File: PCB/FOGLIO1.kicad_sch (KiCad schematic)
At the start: 48 parts, among them J2 USB_C_Receptacle_PowerOnly_6P, J3 6871XX182122_687110182122, J5 Conn_01x03_Pin, J7 Conn_01x07_Pin, U1 TPD2E2U06DCK, U2 ADS131M08xPBS, U3 74LVC1G17, U4 LM27762, U5 AD7606

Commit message: Swap AD7606 for ADS131M08, rework analog front-end and USB input
Schematic-only changes; the PCB has not been updated from the schematic
yet. PCB/CHANGELOG-2026-09-28-ADC-swap.md has the per-part details: every
added/removed part with its pin-to-net list, the netlist diff (before ->
after) and the ERC counts.

1. ADC swap (FOGLIO1)
- Remove the AD7606 (U5) and parts that only served it: C29-C32, C45-C47,
  BUSY LED D3/R8 and the old 1x07 J7.
- Wire up the ADS131M08 (U2): internal 1.2 V reference with 100n on REFIN,
  XTAL2 no-connect, AINxN tied to GND.
- Per-channel divider + anti-alias RC (R61-R76 1.1k/1k, C48-C55 10n C0G):
  op-amp swing +-2.45 V -> +-1.17 V for the +-1.2 V ADC full scale,
  fc ~30 kHz. Channel 7 now digitises the sacrificial-sensor output Vsac.
- ADC supply: U7 TPS7A2033 LDO from +5V -> +3.3VA (AVDD), FB1 -> +3V3
  (DVDD, U3, pull-ups). 1.7 V headroom gives full PSRR, which a passive
  filter on raw VBUS could not.
- Clock from the STM32H7 (MCO2, 5.12 MHz, OSR 256 -> 10 kSPS):
  MCU_CLK -> U3 74LVC1G17 Schmitt buffer -> R80 33R -> CLKIN, with R79
  100k pull-down so CLKIN never floats.
- SPI: R81/R82 33R source terminations on DOUT/DRDY, R77/R78 10k pull-ups
  on CS and SYNC/RESET.
- New 2x06 J7 with GND next to CLK and SCLK.
- Vsac brought from the SENSORS sheet through a new sheet pin (plain wire
  on the root sheet).
- FOGLIO1 paper A4 -> A3. PWR_FLAG added on GND (pre-existing ERC error).

2. Op-amp section swap (FOGLIO2)
- U6 and U13, the two quads next to J3, now hold all 8 first stages
  (S1-S7 and S_sac); U11/U12 hold the 7 difference amps. The
  high-impedance sensor traces can now stay short and on F.Cu.
- Section order chosen from the J3/op-amp pad positions so the sensor
  traces can be routed without crossings.
- Spare section U12-D wired as a follower with +IN at GND (previously
  U13-D was left floating).
- Passive references, values and symbol UUIDs are unchanged, so the PCB
  footprints stay linked.

3. SENSORS sheet readability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
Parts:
- removed C21, C46, C47: 10u, Capacitor_SMD:C_0805_2012Metric, symbol Device:C
- removed C29, C30, C31, C32: 100n, Capacitor_SMD:C_0603_1608Metric, symbol Device:C_Small
- removed C45: 1u, Capacitor_SMD:C_0603_1608Metric, symbol Device:C
- removed D3: LED, LED_SMD:LED_0603_1608Metric, symbol Device:LED
- removed J7: Conn_01x07_Pin, Connector_PinHeader_2.54mm:PinHeader_1x07_P2.54mm_Vertical_SMD_Pin1Right, symbol Connector:Conn_01x07_Pin
- removed R8: 4.7k, Resistor_SMD:R_0603_1608Metric, symbol Device:R
- removed U5: AD7606, Package_QFP:LQFP-64_10x10mm_P0.5mm, symbol Analog_ADC:AD7606
- added C48, C49, C50, C51, C52, C53, C54, C55: 10n C0G, Capacitor_SMD:C_0603_1608Metric, symbol Device:C_Small
- added C58, C59: 100n, Capacitor_SMD:C_0603_1608Metric, symbol Device:C_Small
- added C60, C61: 1u, Capacitor_SMD:C_0603_1608Metric, symbol Device:C_Small
- added C62: 22u 16V, Capacitor_SMD:C_0603_1608Metric, symbol Device:C_Small
- added D1: SMF5.0A, Diode_SMD:D_SMF, symbol Diode:SMF5V0A
- added FB1: BLM18PG221SN1, Inductor_SMD:L_0603_1608Metric, symbol Device:FerriteBead_Small
- added FB2: BLM18KG102SN1, Inductor_SMD:L_0603_1608Metric, symbol Device:FerriteBead_Small
- added J7: Conn_02x06_Odd_Even, Connector_PinHeader_2.54mm:PinHeader_2x06_P2.54mm_Vertical_SMD, symbol Connector_Generic:Conn_02x06_Odd_Even
- added R61, R63, R65, R67, R69, R71, R73, R75: 1.1k, Resistor_SMD:R_0603_1608Metric, symbol Device:R_Small
- added R62, R64, R66, R68, R70, R72, R74, R76: 1k, Resistor_SMD:R_0603_1608Metric, symbol Device:R_Small
- added R77, R78: 10k, Resistor_SMD:R_0603_1608Metric, symbol Device:R_Small
- added R79: 100k, Resistor_SMD:R_0603_1608Metric, symbol Device:R_Small
- added R80, R81, R82: 33R, Resistor_SMD:R_0603_1608Metric, symbol Device:R_Small
- added U7: TPS7A2033PDBVR, Package_TO_SOT_SMD:SOT-23-5, symbol Regulator_Linear:TPS7A20xxxDBV
- U3: footprint (none) -> Package_TO_SOT_SMD:SOT-23-5
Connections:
- net +3V3: now also C36.1, U2.26 (DVDD), C58.1, FB1.2, R77.1, R78.1
- net +5V: now also C60.1, C62.1, D1.1 (A1), FB2.1, U7.1 (IN), U7.3 (EN); no longer C33.1, C34.1, R11.1, R12.1, U4.3 (VIN)
- net GND: now also C48.2, C49.2, C50.2, C51.2, C52.2, C53.2, C54.2, C55.2, C58.2, C59.2, C60.2, C61.2, C62.2, D1.2 (A2), J7.1 (Pin_1), J7.11 (Pin_11), J7.12 (Pin_12), J7.3 (Pin_3), J7.6 (Pin_6), R62.2, R64.2, R66.2, R68.2, R70.2, R72.2, R74.2, R76.2, R79.2, U7.2 (GND)
- net MCU_CLK: now also J7.2 (Pin_2), R79.1
- net Vout1: now also R61.1; no longer U2.29 (AIN0P)
- net Vout2: now also R63.1; no longer U2.32 (AIN1P)
- net Vout3: now also R65.1; no longer U2.1 (AIN2P)
- net Vout4: now also R67.1; no longer U2.4 (AIN3P)
- net Vout5: now also R69.1; no longer U2.5 (AIN4P)
- net Vout6: now also R71.1; no longer U2.8 (AIN5P)
- net Vout7: now also R73.1; no longer U2.9 (AIN6P)
- net Vsac: now also R75.1; no longer U2.12 (AIN7P)
- net at U2.14 (REFIN): now also C59.1
- net +3.3VA: now reaches C37.1, U2.15 (AVDD)
- net +3.3VA: now also C61.1, FB1.1, U7.5 (OUT)
- net ADC_SYNC_RESET: now reaches U2.16 (~{SYNC}/~{RESET})
- net ADC_SYNC_RESET: now also J7.10 (Pin_10), R78.2
- net ADC_CS: now reaches U2.17 (~{CS})
- net ADC_CS: now also J7.8 (Pin_8), R77.2
- net U2_DRDY: now reaches U2.18 (~{DRDY})
- net U2_DRDY: now also R82.1
- net ADC_SCLK: now reaches U2.19 (SCLK)
- net ADC_SCLK: now also J7.4 (Pin_4)
- net U2_DOUT: now reaches U2.20 (DOUT)
- net U2_DOUT: now also R81.1
- net ADC_MOSI: now reaches U2.21 (DIN)
- net ADC_MOSI: now also J7.5 (Pin_5)
- net at U2.23 (XTAL1/CLKIN): now also R80.1; no longer U3.4
- new net: R80.2, U3.4
- new net +5V_CP: C33.1, C34.1, FB2.2, R11.1, R12.1, U4.3 (VIN)
- new net ADC_DRDY: J7.9 (Pin_9), R82.2
- new net ADC_MISO: J7.7 (Pin_7), R81.2
- new net AIN0P: C48.1, R61.2, R62.1, U2.29 (AIN0P)
- new net AIN1P: C49.1, R63.2, R64.1, U2.32 (AIN1P)
- new net AIN2P: C50.1, R65.2, R66.1, U2.1 (AIN2P)
- new net AIN3P: C51.1, R67.2, R68.1, U2.4 (AIN3P)
- new net AIN4P: C52.1, R69.2, R70.1, U2.5 (AIN4P)
- new net AIN5P: C53.1, R71.2, R72.1, U2.8 (AIN5P)
- new net AIN6P: C54.1, R73.2, R74.1, U2.9 (AIN6P)
- new net AIN7P: C55.1, R75.2, R76.1, U2.12 (AIN7P)
- no-connect marks 16 -> 1
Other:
- note added: "+5V -> U7 TPS7A2033 -> +3.3VA (U2 AVDD) +3.3VA -> FB1 -> +3V3 (U2 DVDD, U3, pull-ups)"
- note added: "ADC INPUT DIVIDERS + ANTI-ALIAS (one row per ADS131M08 channel)"
- note added: "ADC SUPPLY (LDO + FERRITE)"
- note added: "J7 -> STM32H7 (3.3 V logic) MCU_CLK: 5.12 MHz from H7 MCO2 (PC9), 40-60 % duty -> U3 Schmitt buffer -> R80 -> ADC CLKIN (10 kSPS @ OSR 256) ADC_SCLK/MOSI/MISO/CS: SPI mode 1 (CPOL 0, CPHA 1), ~8 MHz, SPI clock from the same PLL as MCO2 (synchronous) ADC_DRDY: data ready, active low -> DMA read of 10 words ADC_SYNC_RESET: sync / reset (>= 2048 tCLKIN low), active low Fit 33R series R at the H7 sid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"
- note added: "R81/R82: place next to U2 (source termination)"
- note added: "Ratio 1.0k/(1.1k+1.0k) = 0.476 -> op-amp ±2.45 V maps to ±1.17 V (ADS131M08 FS ±1.2 V). Thevenin 524 Ω + 10 nF C0G -> fc ≈ 30 kHz. AINnN tied to GND at U2 (pseudo-differential). CH7 digitises the sacrificial-sensor output Vsac for diagnostics."
- note added: "USB INPUT: D1 TVS + PI FILTER VBUS (+5V) -> C62 -> FB2 -> +5V_CP (U4 VIN; C34/C33 are the U4-side caps) U7 (ADC LDO), D2/R7 and TP1 stay on +5V (connector side of FB2). Place D1 and C62 right at J2 VBUS/GND pins."
- note removed: "BUSY LED CHECK"
- note removed: "Vdrive = 3v3/5V uC CONVST = instant shoot of output SPI_MISO = bus MISO SPI SPI_CS= bus CS SPI SPI_SCK = bus CK SPI BUSY = if it has level high, the ADC is busy RESET = reset"
- moved on the sheet: C35, C36, C37, U2, U3

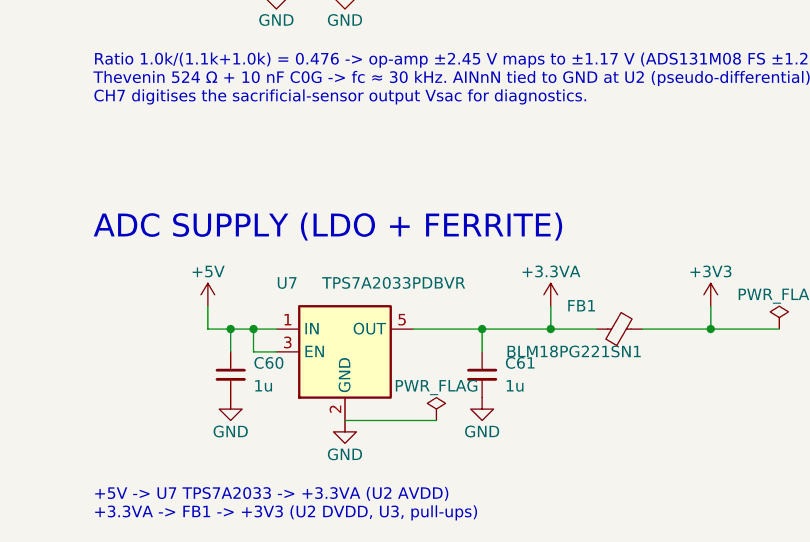
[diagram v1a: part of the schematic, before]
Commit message: Add MPNs to all parts, switch unavailable parts, add Mouser BOM
Schematic procurement pass, based on a Mouser Italia stock/price check
(2026-09-28). The netlist is unchanged and ERC is still at 0 errors.
Details are in PCB/CHANGELOG-2026-09-28-ADC-swap.md, Part 5.

Schematic (FOGLIO1, FOGLIO2):
- Every orderable part (123) now has MPN and Manufacturer fields. The
  old SnapEDA "MF" field on the op-amps is replaced by Manufacturer.
- Difference-amp resistors 5k -> 4.99k (R23, R25, R28, R30, R33, R35,
  R40, R41, R43, R45, R50, R51, R55, R60). Exact 5.0k only exists at
  0.1 %/25 ppm for about EUR 1.7. Both halves of each difference amp use
  the same 4.99k/10k pair, so the ratio still matches (gain 2.004).
- U7 TPS7A2033PDBVR (out of stock, 26-week lead) -> LP5907MFX-3.3/NOPB.
  Same SOT-23-5 pinout and footprint (IN 1, GND 2, EN 3, NC 4, OUT 5).
  The symbol is now Regulator_Linear:LP5907MFX-3.3.
- C62 -> Murata GRM219R61C226ME15K, 22 uF 16 V X5R, footprint
  changed to 0805 (the 0603 ZRB part was out of stock until mid-October).
- Precision parts, all 0.1 % / 25 ppm thin film:
  - 1M Rf and 1k: KOA RN73R
  - 4.99k, 10k, 1.1k: Yageo RT0603BRD
- Capacitor MPNs:
  - 15 pF C0G: Samsung CL10C150JB8NNNC (all Murata 0603 parts are NRND)
  - 10 nF: GRM1885C1H103JA01D
  - 100 nF: GRM188R72A104KA35D (previous part obsolete)
  - 1 uF: GRT188R71E105KE13D (previous part obsolete)
  - 4.7 uF: GRT188R61C475KE13D (previous part not orderable)
  - 10 uF 0805: GRJ21BR61E106KE01L
  - 220 nF: GRM188R71E224KA88D
- General-purpose resistors: Yageo RC0603FR-07; 105k is
  AC0603FR-07105KL because the RC part has no stock.

BOM (PCB/bom/BOM_Mouser_2026-09-28.csv):
- 35 lines, 124 parts per board. Each line has quantity, references,
  value, description, manufacturer, MPN, Mouser link, stock and EUR
  price at qty 10/100.
- Priced parts come to about EUR 49 per board at qty 10.

Open points:
- J5 has no MPN yet (needs a 1x03 2.54 mm SMD alternating-pin header).
- Stock not checked for D2, J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
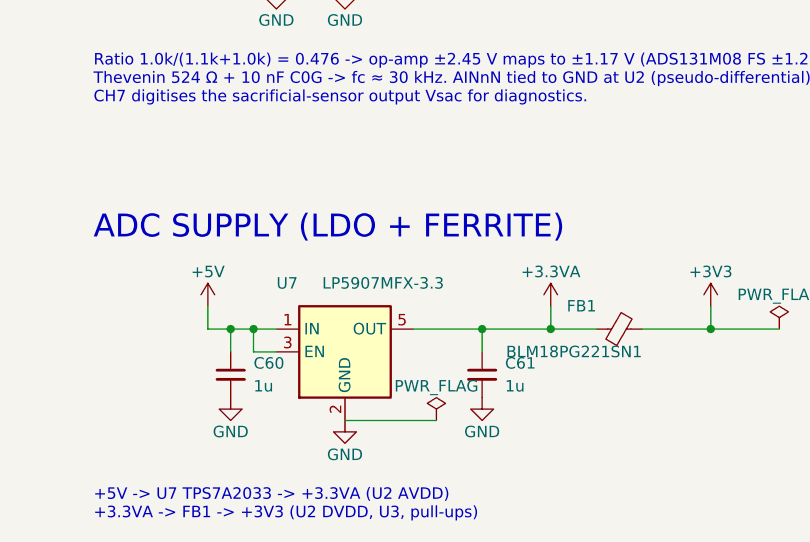
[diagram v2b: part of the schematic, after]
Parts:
- C17, C34: MPN (none) -> GRJ21BR61E106KE01L; Manufacturer (none) -> Murata
- C19, C20: MPN (none) -> GRT188R61C475KE13D; Manufacturer (none) -> Murata
- C33, C58, C59, C7, C9: MPN (none) -> GRM188R72A104KA35D; Manufacturer (none) -> Murata
- C35: MPN (none) -> GRM188R71E224KA88D; Manufacturer (none) -> Murata
- C36, C37, C6, C60, C61: MPN (none) -> GRT188R71E105KE13D; Manufacturer (none) -> Murata
- C48, C49, C50, C51, C52, C53, C54, C55: MPN (none) -> GRM1885C1H103JA01D; Manufacturer (none) -> Murata
- C62: footprint Capacitor_SMD:C_0603_1608Metric -> Capacitor_SMD:C_0805_2012Metric; MF Murata -> (none); MPN ZRB18AR61C226ME01L -> GRM219R61C226ME15K; Manufacturer (none) -> Murata
- D1: MF Littelfuse -> (none); Manufacturer (none) -> Littelfuse
- D2: MPN (none) -> 150060GS75000; Manufacturer (none) -> Würth Elektronik
- FB1: MPN (none) -> BLM18PG221SN1D; Manufacturer (none) -> Murata
- FB2: MF Murata -> (none); Manufacturer (none) -> Murata
- J2: MPN (none) -> USB4125-GF-A; Manufacturer (none) -> GCT
- J3: MF Würth Elektronik -> (none); MPN (none) -> 687110182122; Manufacturer (none) -> Würth Elektronik
- J7: MPN (none) -> 61001221121; Manufacturer (none) -> Würth Elektronik
- R1: MPN (none) -> RC0603FR-07130KL; Manufacturer (none) -> Yageo
- R11, R12, R77, R78: MPN (none) -> RC0603FR-0710KL; Manufacturer (none) -> Yageo
- R2: MPN (none) -> AC0603FR-07105KL; Manufacturer (none) -> Yageo
- R3, R4: MPN (none) -> RC0603FR-075K1L; Manufacturer (none) -> Yageo
- R6: MPN (none) -> RC0603FR-07120KL; Manufacturer (none) -> Yageo
- R61, R63, R65, R67, R69, R71, R73, R75: MPN (none) -> RT0603BRD071K1L; Manufacturer (none) -> Yageo
- R62, R64, R66, R68, R70, R72, R74, R76: MPN (none) -> RN73R1JTTD1001B25; Manufacturer (none) -> KOA Speer
- R7: MPN (none) -> RC0603FR-074K7L; Manufacturer (none) -> Yageo
- R79, R9: MPN (none) -> RC0603FR-07100KL; Manufacturer (none) -> Yageo
- R80, R81, R82: MPN (none) -> RC0603FR-0733RL; Manufacturer (none) -> Yageo
- U1: MPN (none) -> TPD2E2U06DCKR; Manufacturer (none) -> Texas Instruments
- U2: MPN (none) -> ADS131M08IPBSR; Manufacturer (none) -> Texas Instruments
- U3: MPN (none) -> SN74LVC1G17DBVR; Manufacturer (none) -> Texas Instruments
- U4: MPN (none) -> LM27762DSSR; Manufacturer (none) -> Texas Instruments
- U7: value TPS7A2033PDBVR -> LP5907MFX-3.3; symbol Regulator_Linear:TPS7A20xxxDBV -> Regulator_Linear:LP5907MFX-3.3; MPN (none) -> LP5907MFX-3.3/NOPB; Manufacturer (none) -> Texas Instruments

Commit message: Move J5 (sacrificial-sensor select header) to 1.27 mm pitch
J5 (Conn_01x03_Pin: 1 GND, 2 S_sac, 3 S8) selects what drives the
sacrificial-sensor channel. With a jumper, S_sac ties to S8 (the eighth
sensor line from J3) or to GND. At 2.54 mm pitch the header did not fit
next to U13 inside the analog guard, so it moves to the 1.27 mm
equivalent of the same style.

Schematic (FOGLIO1):
- J5 footprint:
  Connector_PinHeader_2.54mm:PinHeader_1x03_P2.54mm_Vertical_SMD_Pin1Right
  -> Connector_PinHeader_1.27mm:PinHeader_1x03_P1.27mm_Vertical_SMD_Pin1Right
- Same alternating "pin 1 right" arrangement, so pin 2 stays on the
  opposite side from pins 1 and 3.
- Pads are 3.0 x 0.65 mm at +/-1.5 mm, 1.27 mm pitch; the courtyard is
  7.0 x 4.82 mm.

Checks:
- Netlist: the only difference is J5's footprint field; every net is
  identical.
- ERC: 0 errors, and the same 31 warnings as before (library-config and
  C_Small symbol-copy warnings).

Docs:
- CHANGELOG: new Part 6 describing the change; the Part 5 note on J5's
  missing MPN now says 1.27 mm and mentions a 1.27 mm shunt.
- BOM: the J5 row points at the 1.27 mm footprint and a 1.27 mm header
  search. The MPN is still to be chosen (search in progress).

Co-Authored-By: Claude Opus 5.5 <noreply@anthropic.com>
Claude-Session: https://claude.ai/code/session_01FkMyFfAWNWvsXoQ2tBz5gZ
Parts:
- J5: footprint Connector_PinHeader_2.54mm:PinHeader_1x03_P2.54mm_Vertical_SMD_Pin1Right -> Connector_PinHeader_1.27mm:PinHeader_1x03_P1.27mm_Vertical_SMD_Pin1Right
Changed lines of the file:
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@@
 			)
 		)
-		(property "Footprint" "Connector_PinHeader_2.54mm:PinHeader_1x03_P2.54mm_Vertical_SMD_Pin1Right"
+		(property "Footprint" "Connector_PinHeader_1.27mm:PinHeader_1x03_P1.27mm_Vertical_SMD_Pin1Right"
 			(at 91.44 113.03 0)
 			(hide yes)

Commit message: Choose J5 header (Harwin M50-3630342) and shunt (M50-2000005)
J5 (sacrificial-sensor select: S_sac to S8 or GND) moved to the 1.27 mm
PinHeader_1x03_P1.27mm_Vertical_SMD_Pin1Right footprint in d276d8f, but
no part number had been chosen for it yet.

Header: Harwin M50-3630342 (Archer M50, 1x03, 1.27 mm, vertical SMT;
Mouser 855-M50-3630342).
- Tails alternate sides.
- The datasheet land pattern (DRG-02647) is 0.65 x 3.00 mm pads, 6.00 mm
  span, 1.27 mm pitch, which matches the KiCad footprint exactly.
- The part has no pin-1 marking. With 3 pins, a 180 degree turn only
  swaps pins 1 and 3, so either way round fits.
- M50-3530342 is the through-hole version and must not be ordered.

Shunt: Harwin M50-2000005 (1.27 mm jumper socket with handle, black;
Mouser 855-M50-2000005). It is made for the M50 0.4 mm square posts. The
red version is M50-2020005.

Changes:
- FOGLIO1: J5 gets MPN, Manufacturer and Datasheet fields. Nets are
  unchanged; ERC is 0 errors with the same 31 warnings.
- BOM: the J5 row is filled in, plus a separate "(J5 jumper)" row for
  the shunt, since it is not a schematic part.
- CHANGELOG Part 6 records the choice.

Stock and price are from an aggregator and Farnell; Mouser blocked
automated reads. They are marked "not verified" in the BOM, so recheck
on mouser.it before ordering.

Co-Authored-By: Claude Opus 5.5 <noreply@anthropic.com>
Claude-Session: https://claude.ai/code/session_01FkMyFfAWNWvsXoQ2tBz5gZ
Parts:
- J5: MPN (none) -> M50-3630342; Manufacturer (none) -> Harwin
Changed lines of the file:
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@@
 			)
 		)
-		(property "Datasheet" ""
+		(property "Datasheet" "https://content.harwin.com/asset/83ac22db-c414-41b6-9c7c-31bf0ab91f55/DRG-02647-Technical-Drawing-Datasheet-M50-363-pdf.pdf"
 			(at 91.44 113.03 0)
 			(hide yes)
@@
 			(at 91.44 113.03 0)
 			(hide yes)
+			(show_name no)
+			(do_not_autoplace no)
+			(effects
+				(font
+					(size 1.27 1.27)
+				)
+			)
+		)
+		(property "MPN" "M50-3630342"
+			(at 91.44 113.03 0)
+			(hide yes)
+			(show_name no)
+			(do_not_autoplace no)
+			(effects
+				(font
+					(size 1.27 1.27)
+				)
+			)
+		)
+		(property "Manufacturer" "Harwin"
+			(at 91.44 113.03 0)
+			(hide yes)

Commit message: Rotate AIN1-AIN3 channel mapping and route Vout2-Vout4
Each U11 output can only leave the op-amp in one practical direction,
and that fixes the order the Vouts arrive at the divider block. Top to
bottom they arrive as Vout1, Vout4, Vout2, Vout3:
- Vout4 leaves pin 16 cleanly on F.Cu at the top.
- Vout3 can only go down and to the right from pin 10, because the D3P
  fan-out via blocks the way up.
- Vout2 is boxed in by the Q2/Q3 vias and must use B.Cu.

Keeping the old mapping would have cost 3-4 extra vias plus a 0.65 mm
squeeze that crosses an AIN line. The firmware has not been written yet,
so the rotation only costs a lookup table there.

Schematic (FOGLIO1): the three hierarchical labels at the divider inputs
are renamed. The names stay the set {Vout2, Vout3, Vout4}, so the sheet
pins and root global labels are untouched.
- R63 (AIN1P): Vout2 -> Vout4
- R65 (AIN2P): Vout3 -> Vout2
- R67 (AIN3P): Vout4 -> Vout3
The divider note on the sheet now carries the full map for the firmware:
  AIN0=Vout1 AIN1=Vout4 AIN2=Vout2 AIN3=Vout3
  AIN4=Vout5 AIN5=Vout6 AIN6=Vout7 AIN7=Vsac
Netlist: only those three nets change. ERC is 0 errors with the same 31
warnings. CHANGELOG Part 7 has the details.

PCB (after Update PCB from Schematic; 0.1 mm):
- Vout4 -> R63: F.Cu from U11 pin 16, between the pins and the D4P
  fan-out, through the R62/C50 gap at y 96.16. No via.
- Vout3 -> R67: F.Cu from pin 10, down and to the right at 45 degrees,
  clear of the D3P via, through the R66/C52 gap at y 100.86. No via.
- Vout2 -> R65: B.Cu from its fan-out via at R29, along y 102.9 below
  U11's bottom resistor row, up at x 155.26, into a via-in-pad at R65.

DRC (trial with the nets swapped on a copy, then re-checked on the saved
board): unconnected items 92 -> 89, with no new violations. Vout1-7 are
now all connected; only Vsac -> R75 remains.

Co-Authored-By: Claude Opus 5.5 <noreply@anthropic.com>
Claude-Session: https://claude.ai/code/session_01FkMyFfAWNWvsXoQ2tBz5gZ
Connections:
- net Vout2: now also R65.1; no longer R63.1
- net Vout3: now also R67.1; no longer R65.1
- net Vout4: now also R63.1; no longer R67.1
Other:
- note added: "Ratio 1.0k/(1.1k+1.0k) = 0.476 -> op-amp ±2.45 V maps to ±1.17 V (ADS131M08 FS ±1.2 V). Thevenin 524 Ω + 10 nF C0G -> fc ≈ 30 kHz. AINnN tied to GND at U2 (pseudo-differential). CH7 digitises the sacrificial-sensor output Vsac for diagnostics. Channel map (set by the PCB routing): AIN0=Vout1, AIN1=Vout4, AIN2=Vout2, AIN3=Vout3, AIN4=Vout5, AIN5=Vout6, AIN6=Vout7, AIN7=Vsac."
- note removed: "Ratio 1.0k/(1.1k+1.0k) = 0.476 -> op-amp ±2.45 V maps to ±1.17 V (ADS131M08 FS ±1.2 V). Thevenin 524 Ω + 10 nF C0G -> fc ≈ 30 kHz. AINnN tied to GND at U2 (pseudo-differential). CH7 digitises the sacrificial-sensor output Vsac for diagnostics."
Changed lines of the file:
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@@
 		)
 	)
-	(text "Ratio 1.0k/(1.1k+1.0k) = 0.476 -> op-amp ±2.45 V maps to ±1.17 V (ADS131M08 FS ±1.2 V).\nThevenin 524 Ω + 10 nF C0G -> fc ≈ 30 kHz. AINnN tied to GND at U2 (pseudo-differential).\nCH7 digitises the sacrificial-sensor output Vsac for diagnostics."
+	(text "Ratio 1.0k/(1.1k+1.0k) = 0.476 -> op-amp ±2.45 V maps to ±1.17 V (ADS131M08 FS ±1.2 V).\nThevenin 524 Ω + 10 nF C0G -> fc ≈ 30 kHz. AINnN tied to GND at U2 (pseudo-differential).\nCH7 digitises the sacrificial-sensor output Vsac for diagnostics.\nChannel map (set by the PCB routing): AIN0=Vout1, AIN1=Vout4, AIN2=Vout2, AIN3=Vout3,\nAIN4=Vout5, AIN5=Vout6, AIN6=Vout7, AIN7=Vsac."
 		(exclude_from_sim no)
 		(at 297.18 172.72 0)
@@
 		)
 	)
-	(hierarchical_label "Vout2"
+	(hierarchical_label "Vout4"
 		(shape input)
 		(at 304.8 66.04 180)
@@
 		)
 	)
-	(hierarchical_label "Vout4"
+	(hierarchical_label "Vout3"
 		(shape input)
 		(at 304.8 96.52 180)
@@
 		)
 	)
-	(hierarchical_label "Vout3"
+	(hierarchical_label "Vout2"
 		(shape input)
 		(at 304.8 81.28 180)
